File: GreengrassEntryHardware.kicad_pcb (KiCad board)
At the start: 2 copper layers, 66 x 57 mm, 29 parts, among them J1 USB_B_Micro, J2 GPIOBreakout, J3 Raspberry_Pi_2_3, J4 AutomaticSlidingDoor, J5 MFRC-522, J6 IndicatorLED, U1 CH340G, Y1 12MHZ

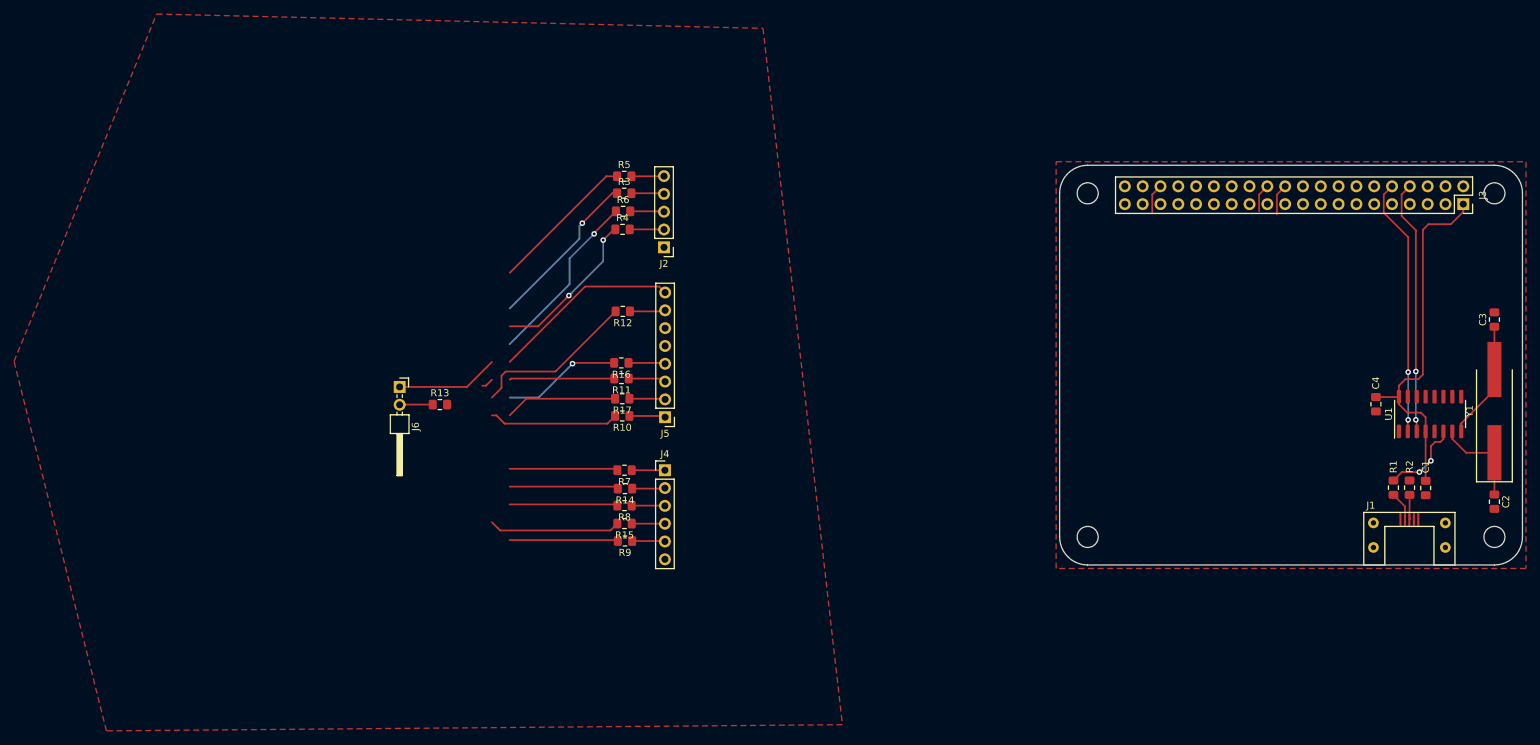
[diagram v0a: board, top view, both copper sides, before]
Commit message: Added GPIO breakout to pcb
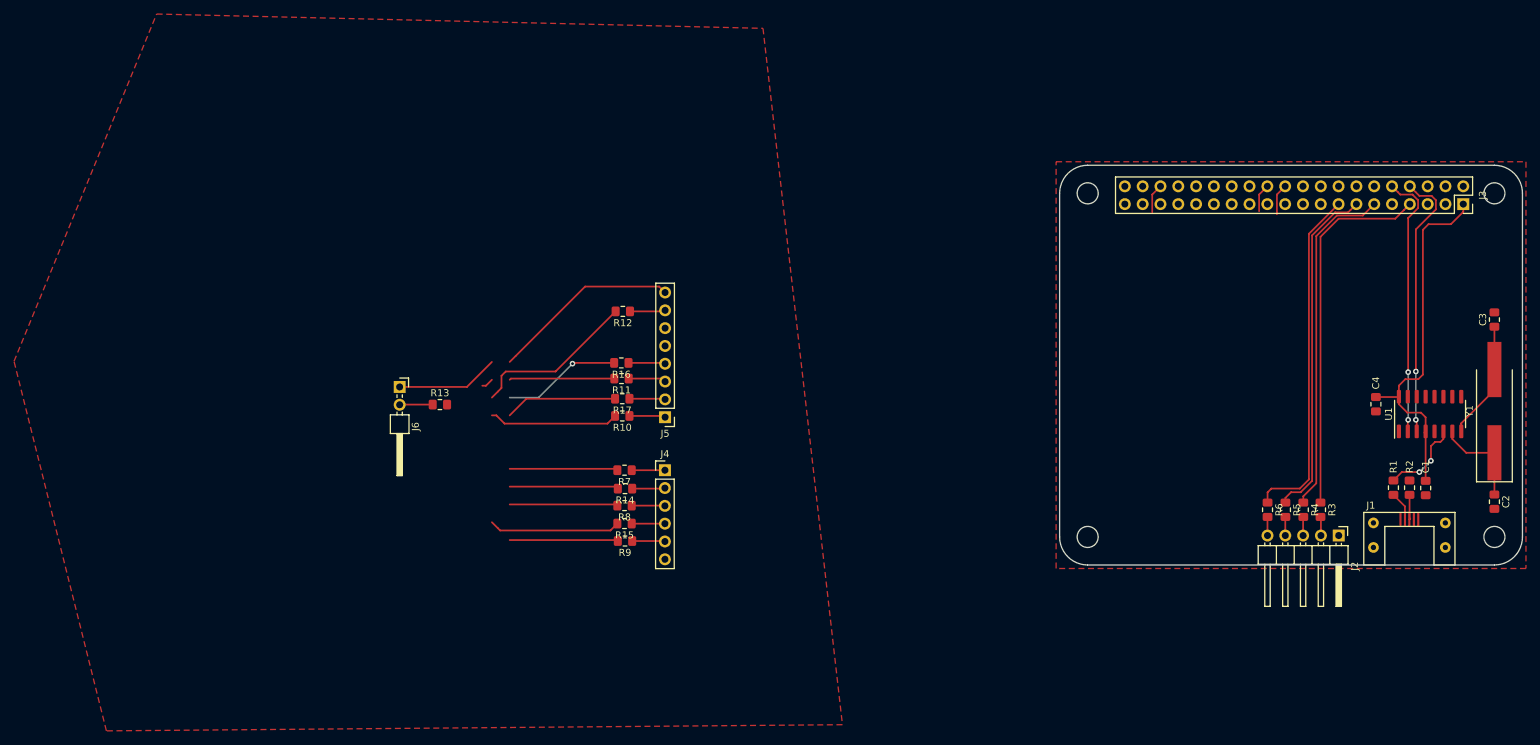
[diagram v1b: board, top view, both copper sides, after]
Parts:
- J2: footprint Connector_PinHeader_2.54mm:PinHeader_1x05_P2.54mm_Vertical -> Connector_PinHeader_2.54mm:PinHeader_1x05_P2.54mm_Horizontal
- moved R3 107.3 mm to (221.2, 100.1), turned to 270 degrees
- moved R4 105.9 mm to (218.8, 100.1), turned to 270 degrees
- moved J2 104.6 mm to (223.8, 103.8), turned to 270 degrees
- moved R5 104.5 mm to (216.2, 100.1), turned to 270 degrees
- moved R6 103.3 mm to (213.7, 100.1), turned to 270 degrees
- renumbered R4 to R3, R6 to R4, R3 to R5, R5 to R6
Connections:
- R3 pad 1: Net-(J3-Pad13) -> Net-(J3-Pad7)
- R4 pad 1: Net-(J3-Pad15) -> Net-(J3-Pad11)
- R5 pad 1: Net-(J3-Pad11) -> Net-(J3-Pad13)
- R6 pad 1: Net-(J3-Pad7) -> Net-(J3-Pad15)
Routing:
- net Net-(J3-Pad7): track 21.0 -> 52.6 mm
- net Net-(J3-Pad13): track 22.6 -> 48.6 mm, vias 2 -> 0
- net Net-(J3-Pad11): track 23.2 -> 48.9 mm, vias 1 -> 0
- net Net-(J3-Pad15): track 25.2 -> 49.1 mm, vias 1 -> 0
- net Net-(J3-Pad8): track 36.3 -> 38.7 mm
- net Net-(J2-Pad2): track 4.90 -> 2.67 mm
- net Net-(J2-Pad3): track 4.83 -> 2.66 mm
- net Net-(J2-Pad4): track 4.69 -> 2.66 mm
- net Net-(J2-Pad5): track 4.66 -> 2.65 mm
- net Net-(J3-Pad10): track 36.9 -> 38.1 mm

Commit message: Tidied up the mfrc pcb layout
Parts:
- removed J6: IndicatorLED, Connector_PinHeader_2.54mm:PinHeader_2x01_P2.54mm_Horizontal
- added R18: 27, Resistor_SMD:R_0805_2012Metric_Pad1.15x1.40mm_HandSolder, F.Cu at (210.6, 95.2)
- J5: footprint Connector_PinHeader_2.54mm:PinHeader_1x08_P2.54mm_Vertical -> Connector_PinHeader_2.54mm:PinHeader_2x05_P2.54mm_Horizontal
- R13: value 100 -> 27
- moved R13 118.1 mm to (213.2, 95.2), turned to 90 degrees
- moved R17 104.9 mm to (225.9, 95.3), turned to 90 degrees
- moved R10 102.2 mm to (223.4, 95.3), turned to 90 degrees
- moved R16 101.1 mm to (221.3, 95.3), turned to 90 degrees
- moved R11 98.6 mm to (219.2, 95.3), turned to 90 degrees
- moved R12 97.0 mm to (215.8, 95.2), turned to 90 degrees
- moved J5 96.8 mm to (223.4, 101.4), turned to 270 degrees
- moved R7 82.2 mm to (203.9, 100.5), turned to 90 degrees
- moved J4 79.6 mm to (206.5, 106.2), turned to 270 degrees
- moved R14 79.3 mm to (201.3, 100.5), turned to 90 degrees
- moved R8 76.9 mm to (198.9, 100.5), turned to 90 degrees
- moved R15 74.4 mm to (196.3, 100.5), turned to 90 degrees
- moved R9 71.9 mm to (193.8, 100.5), turned to 90 degrees
- moved J2 27.7 mm to (223.8, 76.1)
- moved R3 27.7 mm to (221.2, 72.4)
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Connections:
- J3 pad 16: (no net) -> Net-(J3-Pad16)
- R13 pad 1: Net-(J6-Pad2) -> Net-(J5-Pad9)
- R13 pad 2: GNDD -> Net-(J3-Pad18)
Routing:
- net Net-(J3-Pad16): track 0.00 -> 53.4 mm, vias 0 -> 2
- net Net-(J3-Pad18): track 14.6 -> 53.4 mm, vias 0 -> 2
- net Net-(J3-Pad23): track 16.0 -> 54.2 mm
- net Net-(J3-Pad19): track 15.0 -> 52.8 mm, vias 0 -> 2
- net Net-(J3-Pad17): track 27.0 -> 63.6 mm, vias 0 -> 2
- net Net-(J3-Pad21): track 16.9 -> 52.6 mm, vias 1 -> 2
- net Net-(J3-Pad24): track 22.5 -> 57.0 mm
- net Net-(J3-Pad15): track 49.1 -> 19.2 mm
- net Net-(J3-Pad13): track 48.6 -> 20.1 mm
- net Net-(J3-Pad7): track 52.6 -> 24.9 mm
- net Net-(J3-Pad11): track 48.9 -> 21.2 mm
- net Net-(J3-Pad22): track 28.2 -> 52.1 mm, vias 0 -> 2
- net Net-(J3-Pad36): track 23.1 -> 5.68 mm
- net Net-(J3-Pad37): track 15.5 -> 0.19 mm
- net Net-(J3-Pad33): track 15.4 -> 0.24 mm
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
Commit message: Added the door connector to the pcb
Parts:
- J4: footprint Connector_PinHeader_2.54mm:PinHeader_1x06_P2.54mm_Vertical -> Connector_PinHeader_2.54mm:PinHeader_1x06_P2.54mm_Horizontal
- moved R9 3.41 mm to (193.5, 97.1)
- moved R14 3.41 mm to (201.0, 97.1)
- moved R15 3.36 mm to (195.9, 97.1)
- moved R8 3.34 mm to (198.6, 97.1)
- moved R7 3.34 mm to (203.7, 97.1)
- moved J4 2.44 mm to (206.2, 103.8)
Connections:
- J4 pad 1: Net-(J4-Pad1) -> GNDD
- J4 pad 6: GNDD -> Net-(J4-Pad6)
- R14 pad 1: Net-(J4-Pad2) -> Net-(J4-Pad3)
- R15 pad 1: Net-(J4-Pad4) -> Net-(J4-Pad5)
- R7 pad 1: Net-(J4-Pad1) -> Net-(J4-Pad2)
- R8 pad 1: Net-(J4-Pad3) -> Net-(J4-Pad4)
- R9 pad 1: Net-(J4-Pad5) -> Net-(J4-Pad6)
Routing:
- net Net-(J3-Pad29): track 0.28 -> 49.2 mm
- net Net-(J3-Pad31): track 0.40 -> 44.4 mm
- net Net-(J3-Pad33): track 0.24 -> 41.6 mm
- net Net-(J3-Pad37): track 0.19 -> 41.1 mm
- net Net-(J3-Pad36): track 5.68 -> 43.1 mm
- net Net-(R2-Pad1): track 0.00 -> 8.47 mm, vias 0 -> 2
- net Net-(J4-Pad6): track 0.00 -> 5.71 mm
- net Net-(J4-Pad1): track 4.74 -> 0.00 mm
- net Net-(J4-Pad5): track 4.70 -> 5.82 mm
- net Net-(J4-Pad2): track 4.70 -> 5.69 mm
- net Net-(J4-Pad4): track 4.74 -> 5.69 mm
- net Net-(J4-Pad3): track 4.75 -> 5.69 mm

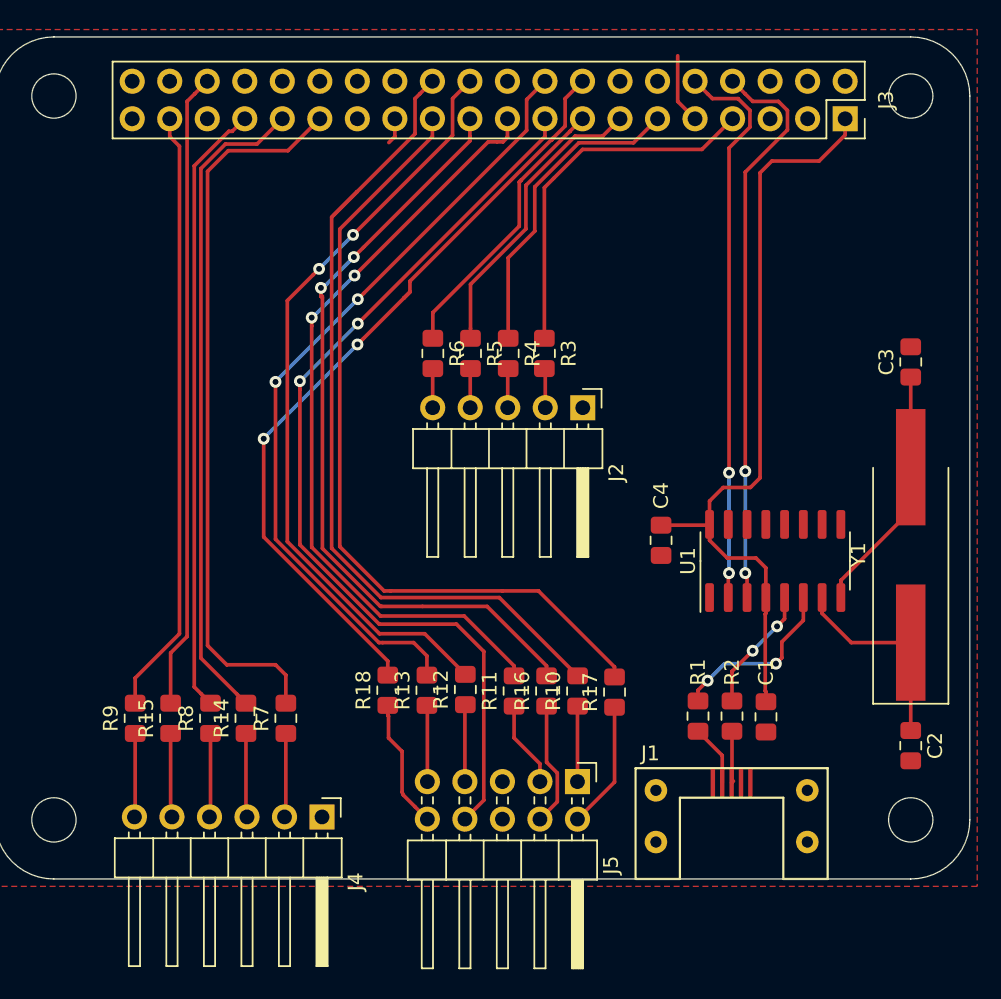
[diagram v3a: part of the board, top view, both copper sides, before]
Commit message: Update schematic and pcb to use Molex SPOX connector for the automatic door
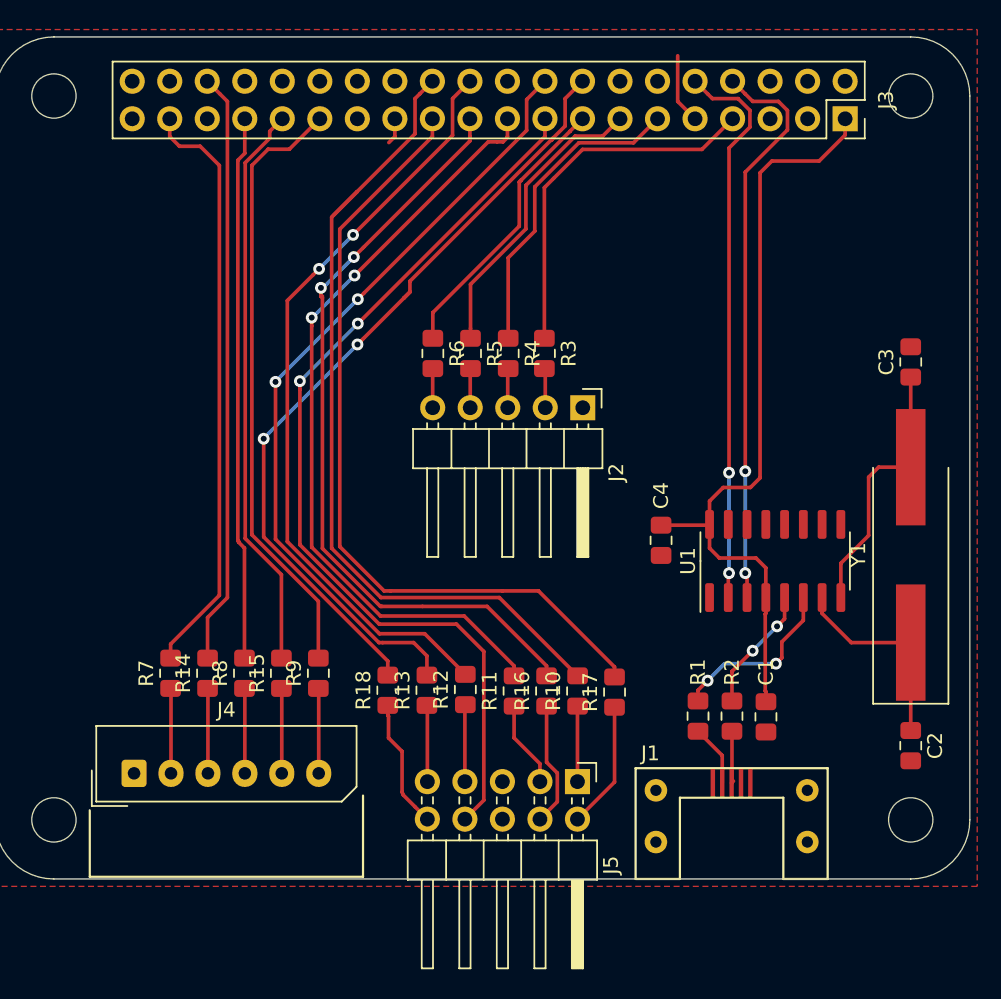
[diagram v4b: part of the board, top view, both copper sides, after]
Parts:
- J4: footprint Connector_PinHeader_2.54mm:PinHeader_1x06_P2.54mm_Horizontal -> GreengrassEntryHardware:Molex_SPOX_5267-06A_1x06_P2.50mm_Horizontal
- moved J4 13.1 mm to (193.4, 100.8), turned to 0 degrees
- moved R9 12.8 mm to (205.9, 94.1)
- moved R7 8.38 mm to (195.9, 94.1)
- moved R15 8.10 mm to (203.4, 94.1)
- moved R14 4.01 mm to (198.4, 94.1)
- moved R8 3.82 mm to (200.9, 94.1)
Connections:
- R14 pad 2: Net-(J3-Pad31) -> Net-(J3-Pad36)
- R15 pad 2: Net-(J3-Pad36) -> Net-(J3-Pad31)
- R7 pad 2: Net-(J3-Pad29) -> Net-(J3-Pad37)
- R9 pad 2: Net-(J3-Pad37) -> Net-(J3-Pad29)
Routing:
- net Net-(J3-Pad29): track 49.2 -> 41.1 mm
- net Net-(J3-Pad31): track 44.4 -> 38.6 mm
- net Net-(J3-Pad33): track 41.6 -> 36.9 mm
- net Net-(J3-Pad36): track 43.1 -> 40.2 mm
- net Net-(C3-Pad1): track 16.9 -> 18.2 mm
- net Net-(J3-Pad37): track 41.1 -> 40.1 mm

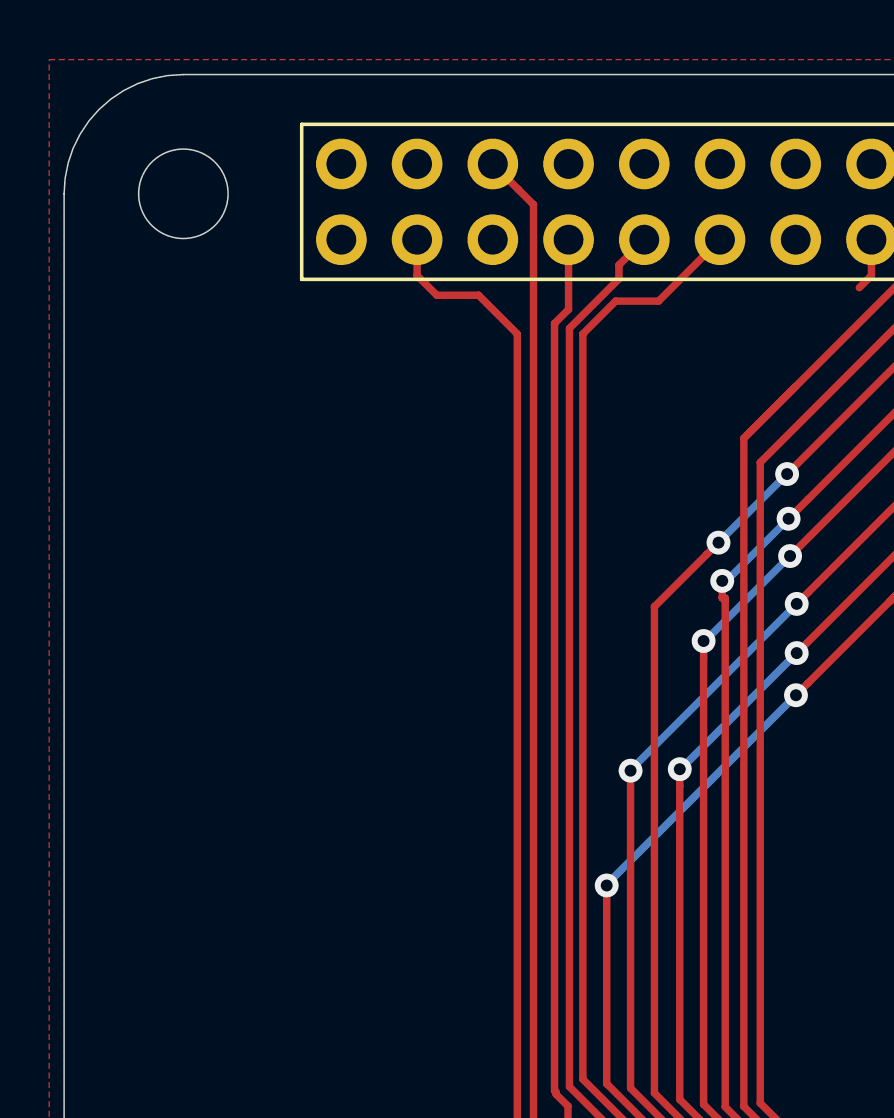
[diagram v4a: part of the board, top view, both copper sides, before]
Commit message: Added a status led
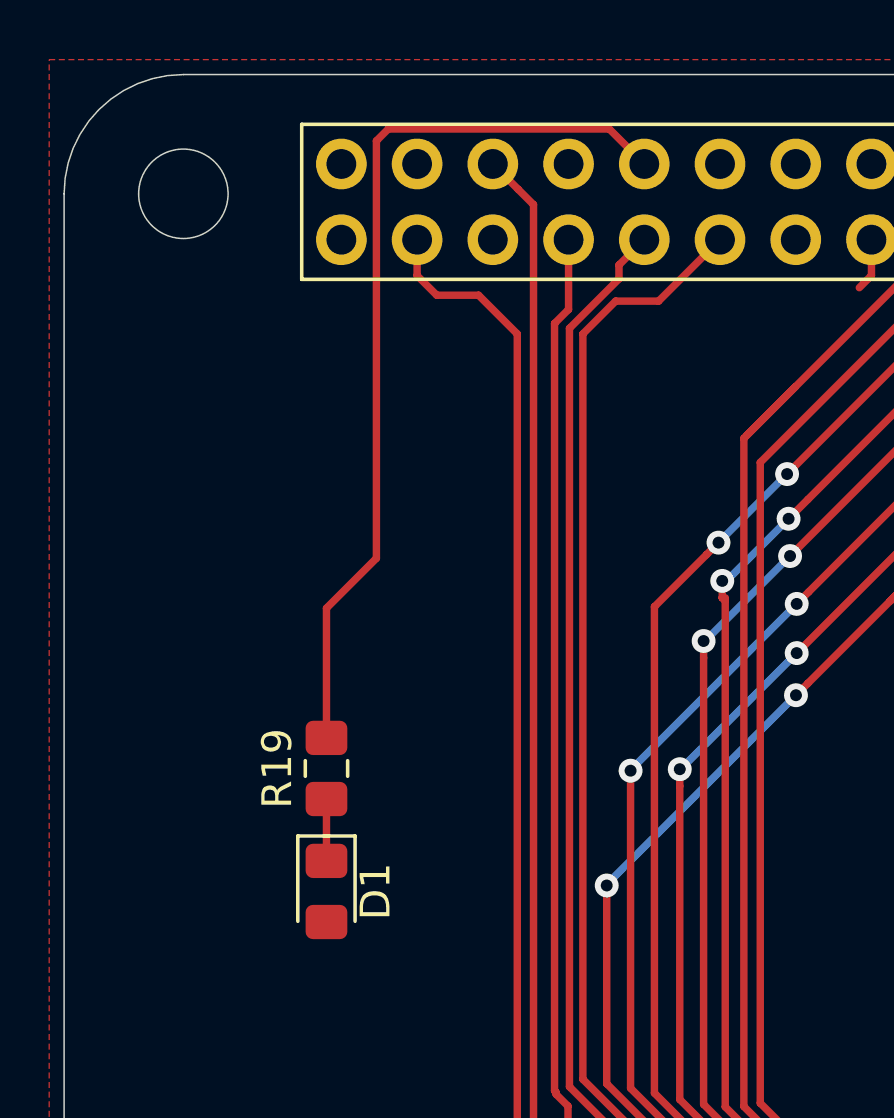
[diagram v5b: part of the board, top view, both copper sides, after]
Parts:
- added D1: LED_ALT, LED_SMD:LED_0805_2012Metric_Pad1.15x1.40mm_HandSolder, F.Cu at (192.8, 78.4)
- added R19: 27, Resistor_SMD:R_0805_2012Metric_Pad1.15x1.40mm_HandSolder, F.Cu at (192.8, 74.3)
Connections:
- J3 pad 32: (no net) -> Net-(J3-Pad32)
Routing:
- net Net-(J3-Pad32): track 0.00 -> 30.4 mm
- net Net-(D1-Pad1): track 0.00 -> 2.08 mm
